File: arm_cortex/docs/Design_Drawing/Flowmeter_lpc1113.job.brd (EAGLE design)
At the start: 160 x 100 mm, 71 parts, among them IC2 OP07CN, IC5 OP07CN, U1 LPC1113FBD48/302,1, U2 LD1117S33CTR, U4 MAX232ACSE+, U5 MAX485CSA+, X1 MKDSN1,5/3-5,08, X2 MKDSN1,5/3-5,08, X3 MKDSN1,5/3-5,08, X4 MKDSN1,5/3-5,08

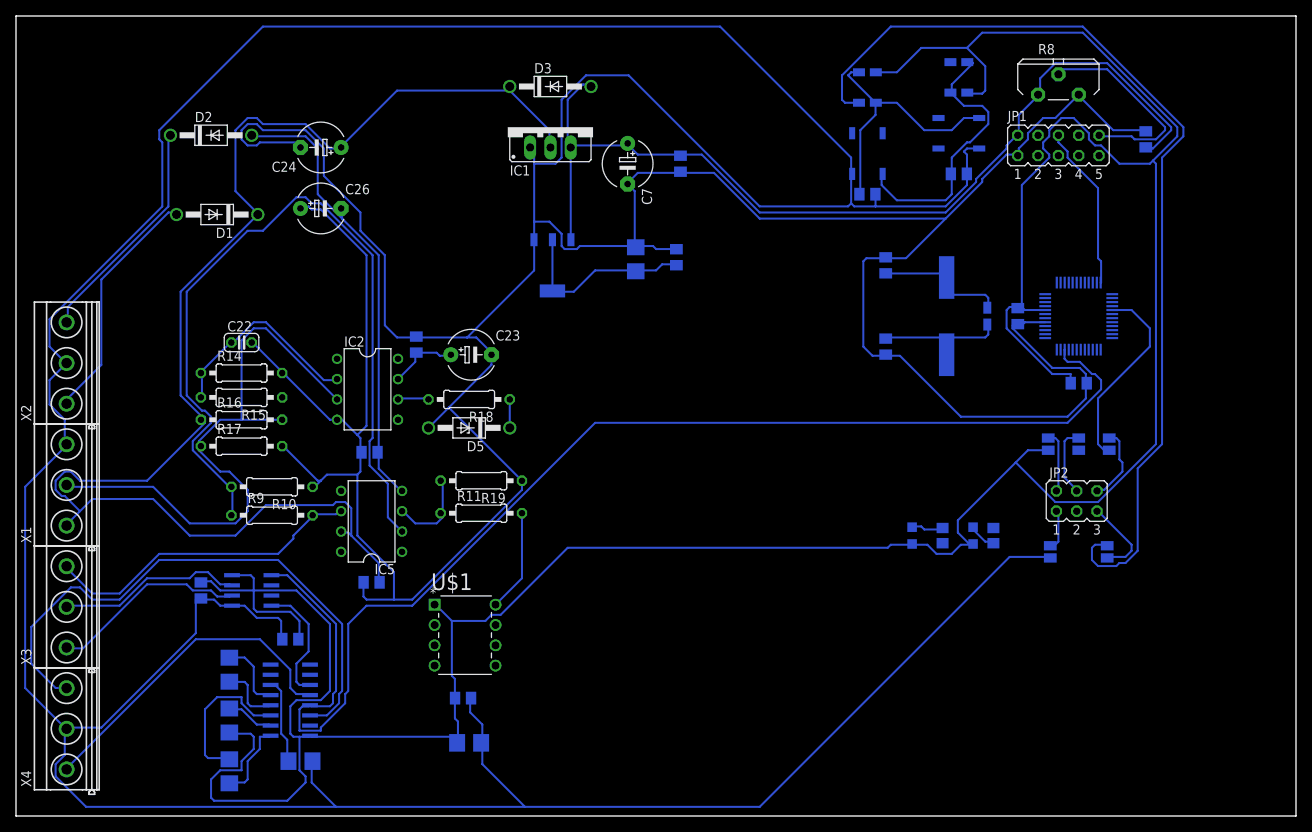
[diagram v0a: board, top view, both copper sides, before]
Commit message: 
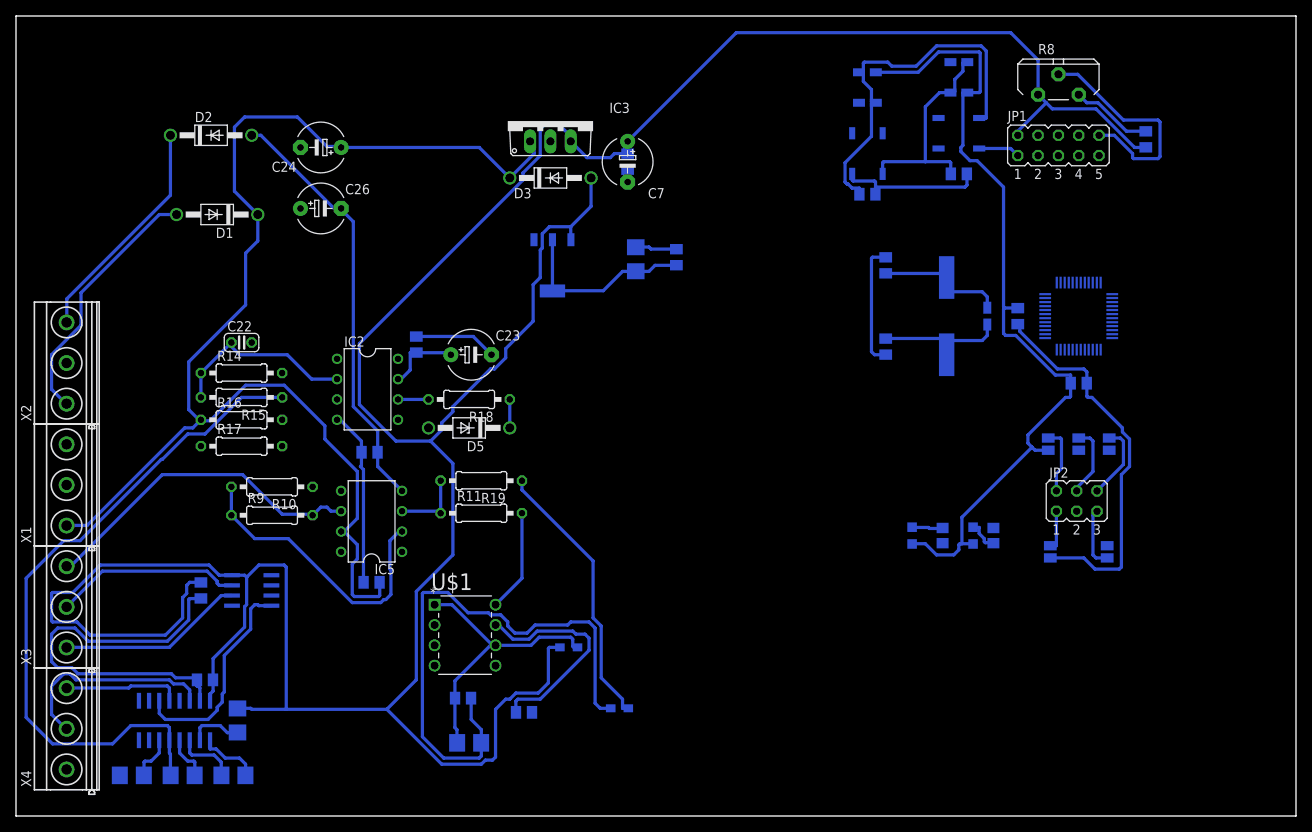
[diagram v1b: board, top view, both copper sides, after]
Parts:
- removed IC1: (no value), v-reg:79XXS
- added C27: 100n, rcl:C0805K
- added IC3: 7805TV, linear:TO220V
- added L1, L2: WURTH ELEKTRONIK - 742792095, wuerth-elektronik:0805
- moved C15 21.2 mm to (14.5, 5.08), turned to 180 degrees
- moved U4 14.7 mm to (19.8, 11.9), turned to 90 degrees
- moved C18 14.4 mm to (20.8, 5.08), turned to 0 degrees
- moved C19 11.8 mm to (23.6, 17.0)
- moved D3 11.4 mm to (66.8, 79.8)
- moved C12 6.61 mm to (76.5, 81.8)
- moved C16 1.02 mm to (27.7, 11.9), turned to 90 degrees
- moved C17 0.72 mm to (27.2, 5.08), turned to 0 degrees
- moved C7 0.25 mm to (76.5, 81.8)
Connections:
- removed net N$18: U$1.7
- removed net N$30: U4.12, X4.1
- removed net N$31: U4.14, X4.3
- new net 5V1: C27.1
- new net GND1: C27.2, U$1.7
- new net N$11: C10.1, C9.+, L2.1, U$1.1, U$1.6
- new net N$12: U4.14, X4.2
- new net N$3: C10.2, C9.-, L1.2
- net +12V: now also IC3.1; no longer IC1.IN
- net 5V: now also C16.-, C19.2, C21.2, IC3.3, L2.2, U4.16, U5.8; no longer IC1.OUT
- net GND: now also IC3.2, L1.1, U4.15, X4.1; no longer C10.2, C9.-, IC1.GND, X4.2
- net LCD_EN: now also U1.43; no longer U1.9
- net LCD_R/W: now also U1.37; no longer U1.17
- net LCD_RS: now also U1.36; no longer U1.30
- net LDAC: now also U1.48; no longer U1.37
- net N$13: now also U4.12, X4.3; no longer U$1.6
- net VCC: no longer C10.1, C16.-, C19.2, C21.2, C9.+, U$1.1, U4.16, U5.8
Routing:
- net GND: track 892.1 -> 220.9 mm
- net VCC: track 392.0 -> 105.3 mm
- net 5V: track 119.0 -> 387.5 mm
- net UART_RX: track 159.6 -> 0.00 mm
- net /RESET: track 121.6 -> 0.00 mm
- net N$27: track 8.90 -> 85.1 mm
- net SENSOR_SIGNAL: track 75.2 -> 0.00 mm
- net N$31: track 71.5 -> 0.00 mm
- net N$3: track 0.00 -> 70.8 mm
- net N$16: track 100.2 -> 37.2 mm
- net N$30: track 41.4 -> 0.00 mm
- net N$11: track 0.00 -> 36.3 mm
- net GND1: track 0.00 -> 27.9 mm
- net N$12: track 0.00 -> 26.3 mm
- net SWDCLK: track 24.5 -> 0.00 mm
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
